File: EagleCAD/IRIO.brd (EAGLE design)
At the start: 13.5 x 11 mm, 17 parts, among them Q2 MOSFET-PCHANNEL, Q3 MOSFET-NCHANNEL

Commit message: Add files via upload
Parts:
- removed C2: (no value), SparkFun-Capacitors:0805
- removed Q2: MOSFET-PCHANNEL, SparkFun-DiscreteSemi:SOT23-3
- removed R3, R5: 10K, SparkFun-Passives:0805
- removed R4: 3K09, SparkFun-Passives:0805
- removed U$5, U$6: SMD-PAD1SMD-PAD80X32, CuriousTech:SMD-PAD6
- moved RC 0.51 mm to (9.40, 9.65)
- moved R1 0.36 mm to (5.84, 6.86)
- moved Q3 0.25 mm to (2.29, 5.84)
- moved C1 0.25 mm to (8.89, 6.86)
- moved LED1 0.25 mm to (2.54, 8.89)
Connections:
- removed net BATT: Q2.2, R5.2, U$5.>PAD
- removed net IO8: R3.1, R4.2, U$6.>PAD
- removed net N$5: Q2.3, R3.2
- removed net N$7: C2.2, Q2.1, R5.1
- net GND: no longer R4.1
- net RX: no longer C2.1
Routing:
- net BATT: track 9.34 -> 0.00 mm
- net IO8: track 4.73 -> 0.00 mm
- net N$7: track 3.95 -> 0.00 mm
- net RX: track 5.54 -> 3.40 mm, vias 1 -> 0
- net N$5: track 1.98 -> 0.00 mm
- net TX: track 7.53 -> 8.04 mm
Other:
- board size 13.5 x 11 mm -> 13.5 x 11.6 mm
- board text removed: "BAT+"
- board text removed: "IO8"

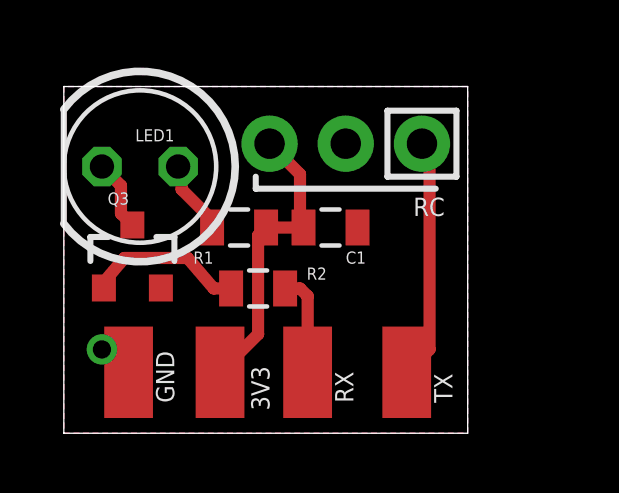
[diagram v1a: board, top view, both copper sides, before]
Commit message: Slimmer design with  TSOP39438
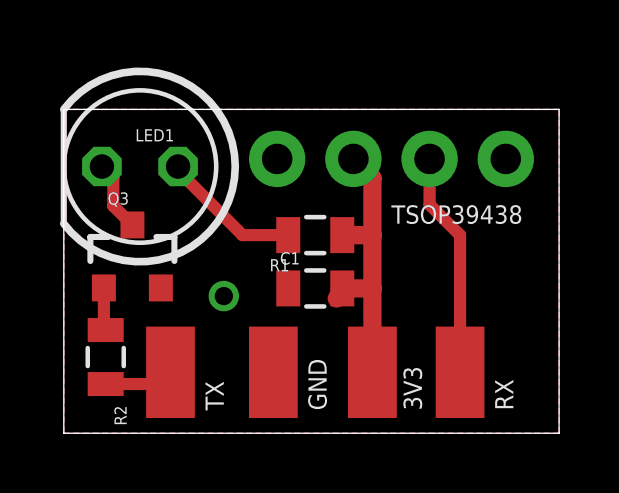
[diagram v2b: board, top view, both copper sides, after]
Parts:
- removed RC: TSSOPxx38, SparkFun-Sensors:BRM-2508
- added TSOP39438: (no value), SparkFun-Connectors:1X04_NO_SILK
- moved R2 5.57 mm to (1.40, 2.54), turned to 90 degrees
- moved U$3 5.08 mm to (10.3, 2.03)
- moved U$2 4.83 mm to (6.99, 2.03)
- moved U$1 4.57 mm to (3.56, 2.03)
- moved R1 2.55 mm to (8.38, 6.60)
- moved C1 2.09 mm to (8.38, 4.83), turned to 180 degrees
- moved U$4 1.78 mm to (13.2, 2.03)
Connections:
- net 3V3: now also TSOP39438.2; no longer RC.3
- net GND: now also TSOP39438.1, TSOP39438.4; no longer RC.2
- net TX: now also TSOP39438.3; no longer RC.1
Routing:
- net N$3: track 5.28 -> 1.41 mm
- net N$2: track 2.50 -> 4.70 mm
- net RX: track 3.40 -> 2.32 mm
- net TX: track 8.04 -> 7.53 mm
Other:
- board size 13.5 x 11.6 mm -> 16.5 x 10.8 mm
- board text added: "CuriousTech.net"

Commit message: Corrected footprint for TSOP39438
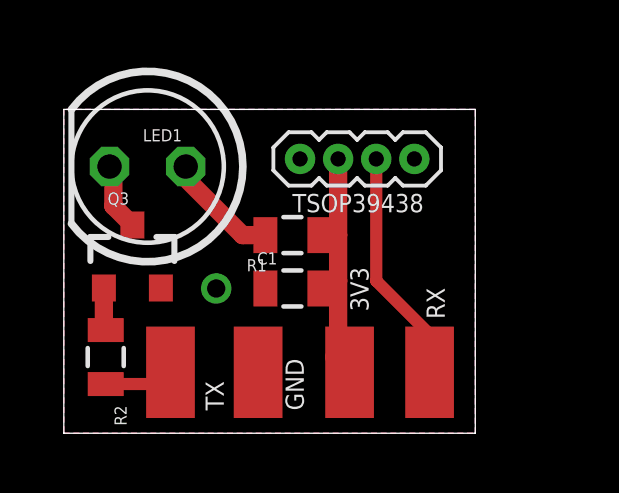
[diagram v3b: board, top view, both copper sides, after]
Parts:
- TSOP39438: device SparkFun-Connectors:1X04_NO_SILK -> SparkFun-Connectors:1X04_1.27MM
- moved U$4 1.02 mm to (12.2, 2.03)
- moved U$3 0.76 mm to (9.53, 2.03)
- moved C1 0.76 mm to (7.62, 4.83)
- moved R1 0.76 mm to (7.62, 6.60)
- moved TSOP39438 0.76 mm to (7.87, 9.14)
- moved U$2 0.51 mm to (6.48, 2.03)
- moved LED1 0.25 mm to (2.79, 8.89)
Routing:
- net 3V3: track 9.77 -> 8.73 mm
- net N$2: track 4.70 -> 3.95 mm
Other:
- board size 16.5 x 10.8 mm -> 13.7 x 10.8 mm
